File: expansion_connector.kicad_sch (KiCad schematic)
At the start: 38 parts, among them J18 ASP-218650-01_mounting_holes, J8 Plug_Samtec_UMPT_1x6_UMPT-06-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, U2 AT24CS01_SOIC8

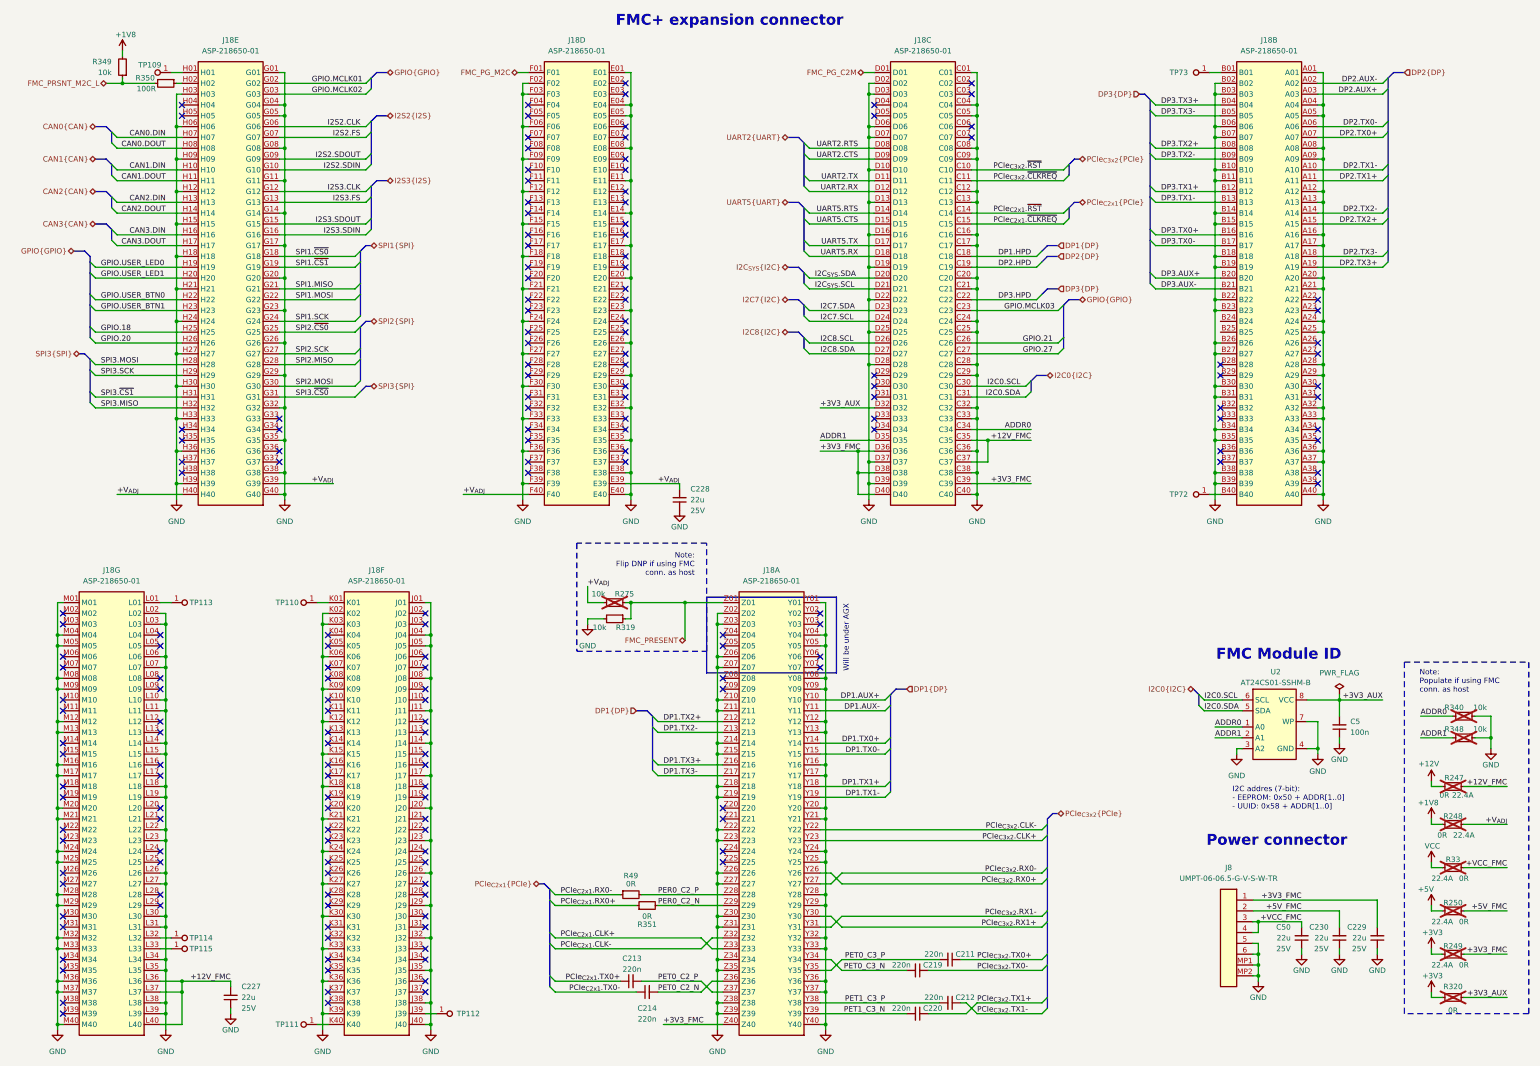
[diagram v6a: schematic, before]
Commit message: [#89536] Replace expansion connectors to achieve 10mm mating height
Used:
ASP-208571-01 (mating: ASP-184329-01 )
UMPT-06-02.5-L-V-S-W-TR (mating: UMPS-06-07.5-L-V-S-W-TR)
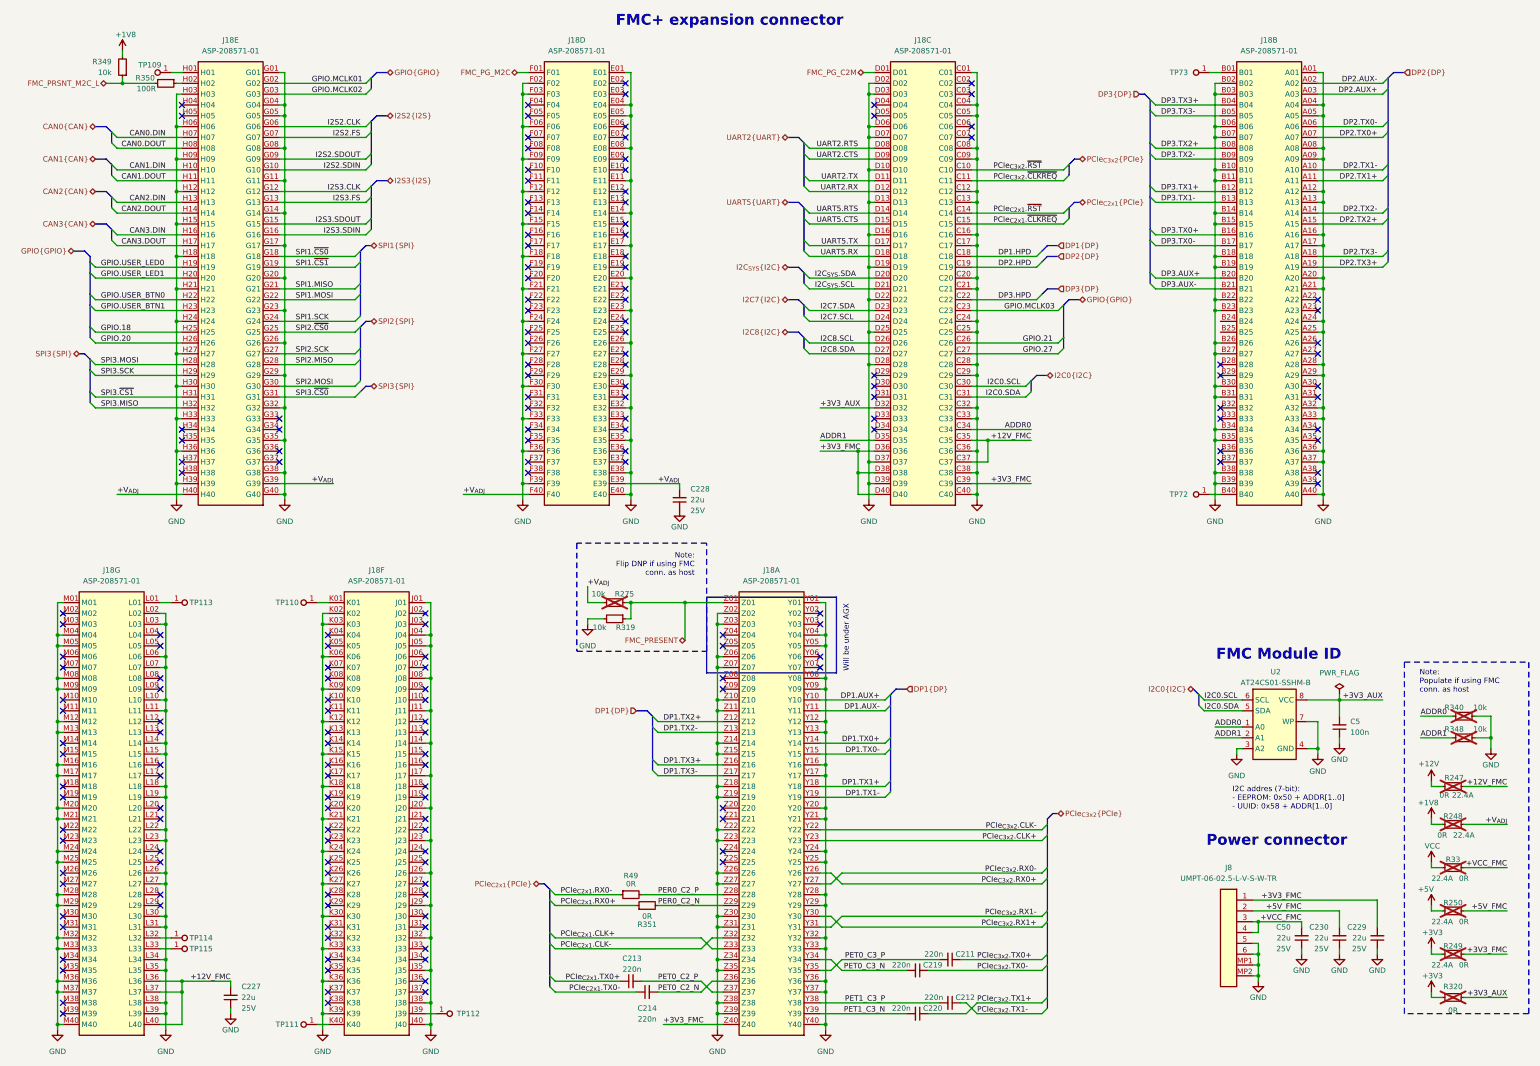
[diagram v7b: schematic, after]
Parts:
- J18: value ASP-218650-01_mounting_holes -> ASP-208571-01_mounting_holes; footprint antmicro-footprints:ASP-218650-01_mounting_holes -> antmicro-footprints:ASP-208571-01_mounting_holes; symbol antmicroB2BConnectors:ASP-218650-01_mounting_holes -> antmicroB2BConnectors:ASP-208571-01_mounting_holes; MPN ASP-218650-01 -> ASP-208571-01
- J8: value Plug_Samtec_UMPT_1x6_UMPT-06-06.5-G-V-S-TR -> Plug_Samtec_UMPT_1x6_UMPT-06-02.5-L-V-S-W-TR; footprint antmicro-footprints:Conn_Plug_Samtec_UMPT_1x6_UMPT-06-06.5-G-V-S-W-TR -> antmicro-footprints:Conn_Plug_Samtec_UMPT_1x6_UMPT-06-02.5-L-V-S-W-TR; symbol antmicroB2BConnectors:Plug_Samtec_UMPT_1x6_UMPT-06-06.5-G-V-S-W-TR -> antmicroB2BConnectors:Plug_Samtec_UMPT_1x6_UMPT-06-02.5-L-V-S-W-TR; MPN UMPT-06-06.5-G-V-S-W-TR -> UMPT-06-02.5-L-V-S-W-TR
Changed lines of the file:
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@@
 	)
 	(symbol
-		(lib_id "antmicroB2BConnectors:ASP-218650-01_mounting_holes")
+		(lib_id "antmicroB2BConnectors:ASP-208571-01_mounting_holes")
 		(at 81.28 153.67 0)
 		(mirror y)
@@
 			)
 		)
-		(property "Value" "ASP-218650-01_mounting_holes"
+		(property "Value" "ASP-208571-01_mounting_holes"
 			(at 44.45 163.83 0)
 			(effects
@@
 			)
 		)
-		(property "Footprint" "antmicro-footprints:ASP-218650-01_mounting_holes"
+		(property "Footprint" "antmicro-footprints:ASP-208571-01_mounting_holes"
 			(at 44.45 166.37 0)
 			(effects
@@
 			)
 		)
-		(property "Datasheet" "https://suddendocs.samtec.com/prints/asp-218650-01-mkt.pdf"
+		(property "Datasheet" "https://suddendocs.samtec.com/prints/asp-208571-01-mkt.pdf"
 			(at 44.45 168.91 0)
 			(effects
@@
 		)
 		(property "Description" "FMC connector"
-			(at 81.28 153.67 0)
+			(at 44.45 179.07 0)
 			(effects
 				(font
 					(size 1.27 1.27)
 				)
+				(justify left bottom)
 				(hide yes)
 			)
 		)
-		(property "MPN" "ASP-218650-01"
+		(property "MPN" "ASP-208571-01"
 			(at 69.85 148.59 0)
 			(effects
@@
 	)
 	(symbol
-		(lib_id "antmicroB2BConnectors:ASP-218650-01_mounting_holes")
+		(lib_id "antmicroB2BConnectors:ASP-208571-01_mounting_holes")
 		(at 109.22 29.21 0)
 		(mirror y)
@@
 			)
 		)
-		(property "Value" "ASP-218650-01_mounting_holes"
+		(property "Value" "ASP-208571-01_mounting_holes"
 			(at 72.39 39.37 0)
 			(effects
@@
 			)
 		)
-		(property "Footprint" "antmicro-footprints:ASP-218650-01_mounting_holes"
+		(property "Footprint" "antmicro-footprints:ASP-208571-01_mounting_holes"
 			(at 72.39 41.91 0)
 			(effects
@@
 			)
 		)
-		(property "Datasheet" "https://suddendocs.samtec.com/prints/asp-218650-01-mkt.pdf"
+		(property "Datasheet" "https://suddendocs.samtec.com/prints/asp-208571-01-mkt.pdf"
 			(at 72.39 44.45 0)
 			(effects
@@
 		)
 		(property "Description" "FMC connector"
-			(at 109.22 29.21 0)
+			(at 72.39 54.61 0)
 			(effects
 				(font
 					(size 1.27 1.27)
 				)
+				(justify left bottom)
 				(hide yes)
 			)
 		)
-		(property "MPN" "ASP-218650-01"
+		(property "MPN" "ASP-208571-01"
 			(at 97.79 24.13 0)
 			(effects
@@
 	)
 	(symbol
-		(lib_id "antmicroB2BConnectors:ASP-218650-01_mounting_holes")
+		(lib_id "antmicroB2BConnectors:ASP-208571-01_mounting_holes")
 		(at 190.5 29.21 0)
 		(mirror y)
@@
 			)
 		)
-		(property "Value" "ASP-218650-01_mounting_holes"
+		(property "Value" "ASP-208571-01_mounting_holes"
 			(at 153.67 39.37 0)
 			(effects
@@
 			)
 		)
-		(property "Footprint" "antmicro-footprints:ASP-218650-01_mounting_holes"
+		(property "Footprint" "antmicro-footprints:ASP-208571-01_mounting_holes"
 			(at 153.67 41.91 0)
 			(effects
@@
 			)
 		)
-		(property "Datasheet" "https://suddendocs.samtec.com/prints/asp-218650-01-mkt.pdf"
+		(property "Datasheet" "https://suddendocs.samtec.com/prints/asp-208571-01-mkt.pdf"
 			(at 153.67 44.45 0)
 			(effects
@@
 		)
 		(property "Description" "FMC connector"
-			(at 190.5 29.21 0)
+			(at 153.67 54.61 0)
 			(effects
 				(font
 					(size 1.27 1.27)
 				)
+				(justify left bottom)
 				(hide yes)
 			)
 		)
-		(property "MPN" "ASP-218650-01"
+		(property "MPN" "ASP-208571-01"
 			(at 179.07 24.13 0)
 			(effects
@@
 	)
 	(symbol
-		(lib_id "antmicroB2BConnectors:ASP-218650-01_mounting_holes")
+		(lib_id "antmicroB2BConnectors:ASP-208571-01_mounting_holes")
 		(at 143.51 153.67 0)
 		(mirror y)
@@
 			)
 		)
-		(property "Value" "ASP-218650-01_mounting_holes"
+		(property "Value" "ASP-208571-01_mounting_holes"
 			(at 106.68 163.83 0)
 			(effects
@@
 			)
 		)
-		(property "Footprint" "antmicro-footprints:ASP-218650-01_mounting_holes"
+		(property "Footprint" "antmicro-footprints:ASP-208571-01_mounting_holes"
 			(at 106.68 166.37 0)
 			(effects
@@
 			)
 		)
-		(property "Datasheet" "https://suddendocs.samtec.com/prints/asp-218650-01-mkt.pdf"
+		(property "Datasheet" "https://suddendocs.samtec.com/prints/asp-208571-01-mkt.pdf"
 			(at 106.68 168.91 0)
 			(effects
@@
 		)
 		(property "Description" "FMC connector"
-			(at 143.51 153.67 0)
+			(at 106.68 179.07 0)
 			(effects
 				(font
 					(size 1.27 1.27)
 				)
+				(justify left bottom)
 				(hide yes)
 			)
 		)
-		(property "MPN" "ASP-218650-01"
+		(property "MPN" "ASP-208571-01"
 			(at 132.08 148.59 0)
 			(effects
@@
 	)
 	(symbol
-		(lib_id "antmicroB2BConnectors:ASP-218650-01_mounting_holes")
+		(lib_id "antmicroB2BConnectors:ASP-208571-01_mounting_holes")
 		(at 353.06 29.21 0)
 		(mirror y)
@@
 			)
 		)
-		(property "Value" "ASP-218650-01_mounting_holes"
+		(property "Value" "ASP-208571-01_mounting_holes"
 			(at 316.23 39.37 0)
 			(effects
@@
 			)
 		)
-		(property "Footprint" "antmicro-footprints:ASP-218650-01_mounting_holes"
+		(property "Footprint" "antmicro-footprints:ASP-208571-01_mounting_holes"
 			(at 316.23 41.91 0)
 			(effects
@@
 			)
 		)
-		(property "Datasheet" "https://suddendocs.samtec.com/prints/asp-218650-01-mkt.pdf"
+		(property "Datasheet" "https://suddendocs.samtec.com/prints/asp-208571-01-mkt.pdf"
 			(at 316.23 44.45 0)
 			(effects
@@
 		)
 		(property "Description" "FMC connector"
-			(at 353.06 29.21 0)
+			(at 316.23 54.61 0)
 			(effects
 				(font
 					(size 1.27 1.27)
 				)
+				(justify left bottom)
 				(hide yes)
 			)
 		)
-		(property "MPN" "ASP-218650-01"
+		(property "MPN" "ASP-208571-01"
 			(at 341.63 24.13 0)
 			(effects
@@
 	)
 	(symbol
-		(lib_id "antmicroB2BConnectors:ASP-218650-01_mounting_holes")
+		(lib_id "antmicroB2BConnectors:ASP-208571-01_mounting_holes")
 		(at 271.78 29.21 0)
 		(mirror y)
@@
 			)
 		)
-		(property "Value" "ASP-218650-01_mounting_holes"
+		(property "Value" "ASP-208571-01_mounting_holes"
 			(at 234.95 39.37 0)
 			(effects
@@
 			)
 		)
-		(property "Footprint" "antmicro-footprints:ASP-218650-01_mounting_holes"
+		(property "Footprint" "antmicro-footprints:ASP-208571-01_mounting_holes"
 			(at 234.95 41.91 0)
 			(effects
@@
 			)
 		)
-		(property "Datasheet" "https://suddendocs.samtec.com/prints/asp-218650-01-mkt.pdf"
+		(property "Datasheet" "https://suddendocs.samtec.com/prints/asp-208571-01-mkt.pdf"
 			(at 234.95 44.45 0)
 			(effects
@@
 		)
 		(property "Description" "FMC connector"
-			(at 271.78 29.21 0)
+			(at 234.95 54.61 0)
 			(effects
 				(font
 					(size 1.27 1.27)
 				)
+				(justify left bottom)
 				(hide yes)
 			)
 		)
-		(property "MPN" "ASP-218650-01"
+		(property "MPN" "ASP-208571-01"
 			(at 260.35 24.13 0)
 			(effects
@@
 	)
 	(symbol
-		(lib_id "antmicroB2BConnectors:Plug_Samtec_UMPT_1x6_UMPT-06-06.5-G-V-S-W-TR")
+		(lib_id "antmicroB2BConnectors:Plug_Samtec_UMPT_1x6_UMPT-06-02.5-L-V-S-W-TR")
 		(at 337.82 223.52 0)
 		(mirror y)
@@
 			)
 		)
-		(property "Value" "Plug_Samtec_UMPT_1x6_UMPT-06-06.5-G-V-S-TR"
+		(property "Value" "Plug_Samtec_UMPT_1x6_UMPT-06-02.5-L-V-S-W-TR"
 			(at 314.96 231.14 0)
 			(effects
@@
 			)
 		)
-		(property "Footprint" "antmicro-footprints:Conn_Plug_Samtec_UMPT_1x6_UMPT-06-06.5-G-V-S-W-TR"
+		(property "Footprint" "antmicro-footprints:Conn_Plug_Samtec_UMPT_1x6_UMPT-06-02.5-L-V-S-W-TR"
 			(at 314.96 233.68 0)
 			(effects
@@
 			)
 		)
-		(property "MPN" "UMPT-06-06.5-G-V-S-W-TR"
+		(property "MPN" "UMPT-06-02.5-L-V-S-W-TR"
 			(at 332.105 218.44 0)
 			(effects
@@
 	)
 	(symbol
-		(lib_id "antmicroB2BConnectors:ASP-218650-01_mounting_holes")
+		(lib_id "antmicroB2BConnectors:ASP-208571-01_mounting_holes")
 		(at 236.22 153.67 0)
 		(mirror y)
@@
 			)
 		)
-		(property "Value" "ASP-218650-01_mounting_holes"
+		(property "Value" "ASP-208571-01_mounting_holes"
 			(at 199.39 163.83 0)
 			(effects
@@
 			)
 		)
-		(property "Footprint" "antmicro-footprints:ASP-218650-01_mounting_holes"
+		(property "Footprint" "antmicro-footprints:ASP-208571-01_mounting_holes"
 			(at 199.39 166.37 0)
 			(effects
@@
 			)
 		)
-		(property "Datasheet" "https://suddendocs.samtec.com/prints/asp-218650-01-mkt.pdf"
+		(property "Datasheet" "https://suddendocs.samtec.com/prints/asp-208571-01-mkt.pdf"
 			(at 199.39 168.91 0)
 			(effects
@@
 		)
 		(property "Description" "FMC connector"
-			(at 236.22 153.67 0)
+			(at 199.39 179.07 0)
 			(effects
 				(font
 					(size 1.27 1.27)
 				)
+				(justify left bottom)
 				(hide yes)
 			)
 		)
-		(property "MPN" "ASP-218650-01"
+		(property "MPN" "ASP-208571-01"
 			(at 224.79 148.59 0)
 			(effects

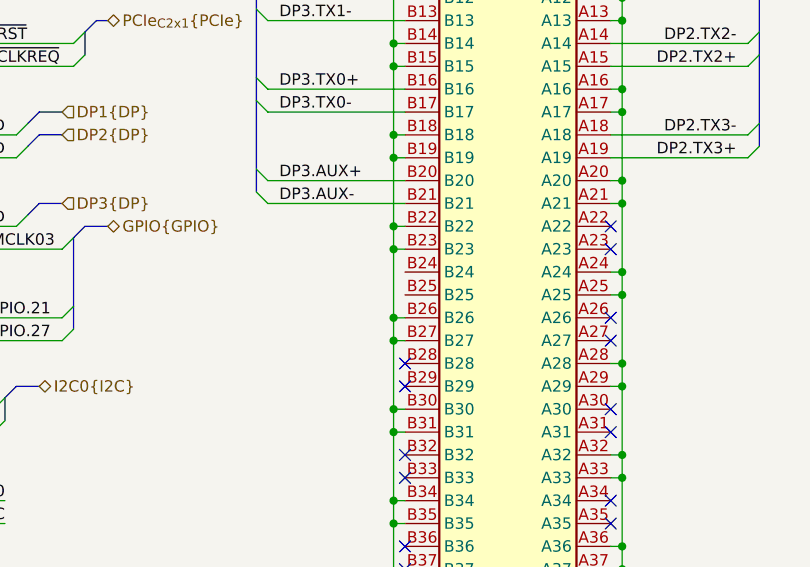
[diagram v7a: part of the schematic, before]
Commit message: [#90793] Add more testpoints on bottom side for ICT, clean DRC
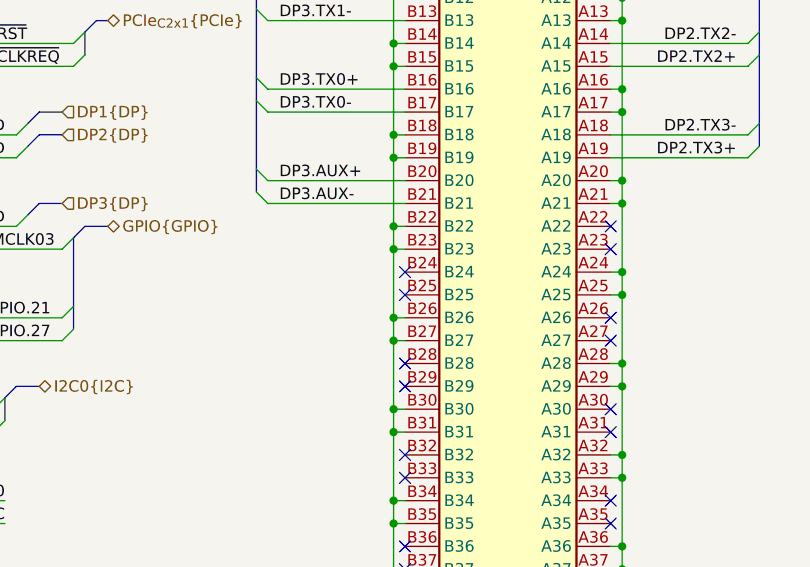
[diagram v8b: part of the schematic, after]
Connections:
- no-connect marks 179 -> 181
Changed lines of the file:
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@@
+	)
+	(no_connect
+		(at 330.2 90.17)
 	)
 	(no_connect
@@
 	)
 	(no_connect
+		(at 330.2 87.63)
+	)
+	(no_connect
